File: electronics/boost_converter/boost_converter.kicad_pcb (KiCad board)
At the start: 2 copper layers, 75 x 40 mm, 30 parts, among them J1 Screw_Terminal_01x02, J2 Conn_01x04_Pin, J3 Screw_Terminal_01x02, U1 MC34063AP

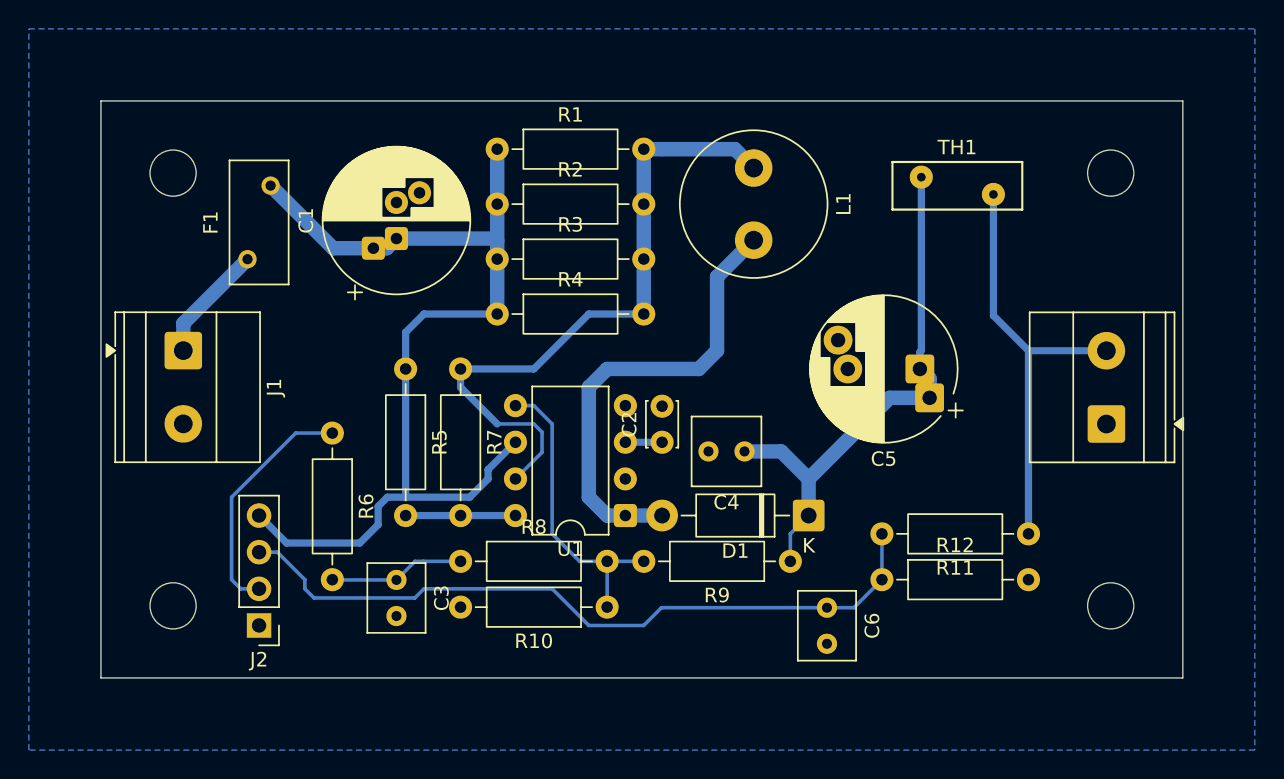
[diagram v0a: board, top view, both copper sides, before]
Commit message: silk screen optimized; drc ok
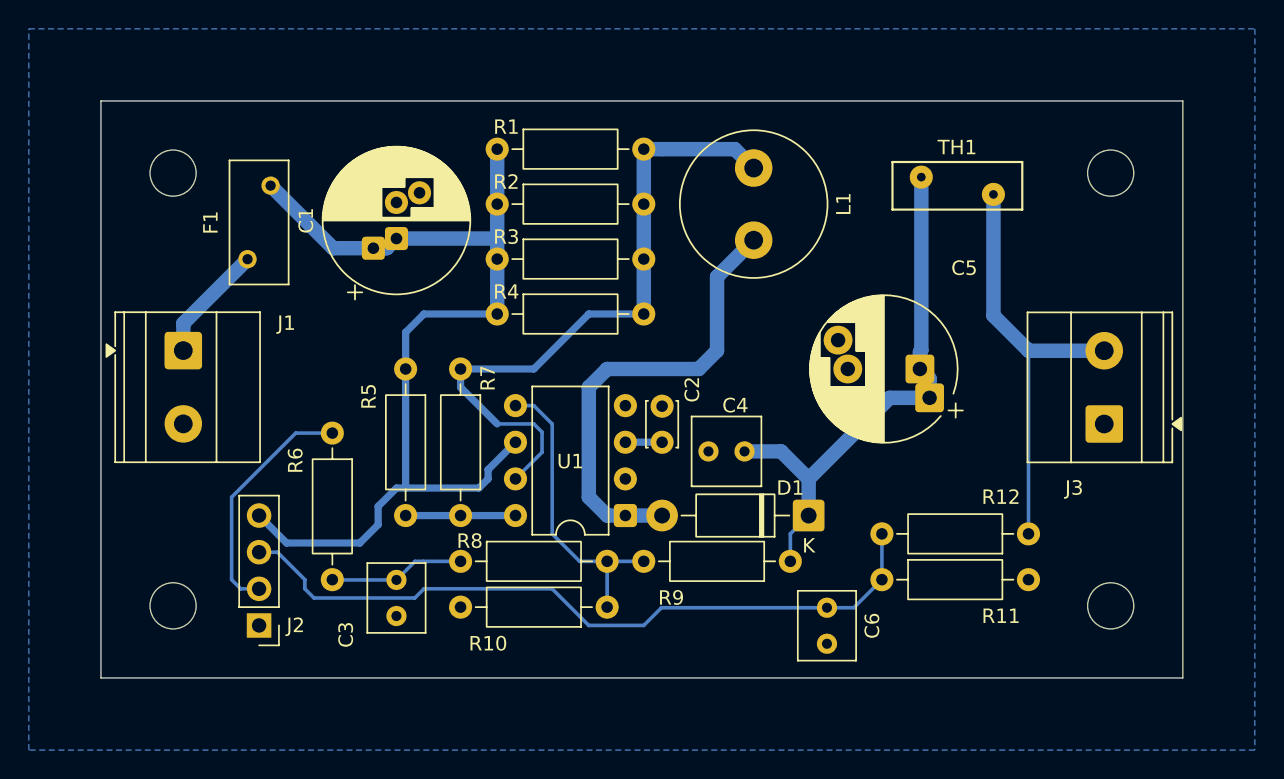
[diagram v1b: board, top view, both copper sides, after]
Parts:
- moved J3 0.15 mm to (119.6, 72.4)
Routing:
- net VCC: track 70.2 -> 69.5 mm
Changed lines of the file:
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@@
 		(tags "Resistor Axial_DIN0207 series Axial Horizontal pin pitch 10.16mm 0.25W = 1/4W length 6.3mm diameter 2.5mm")
 		(property "Reference" "R10"
-			(at 5.08 -2.37 0)
+			(at 8.255 -2.54 0)
 			(layer "F.SilkS")
 			(effects
@@
 		(tags "Resistor Axial_DIN0207 series Axial Horizontal pin pitch 10.16mm 0.25W = 1/4W length 6.3mm diameter 2.5mm")
 		(property "Reference" "R1"
-			(at 5.08 -2.37 0)
+			(at 0.635 -1.524 0)
 			(layer "F.SilkS")
 			(effects
@@
 		(tags "Resistor Axial_DIN0207 series Axial Horizontal pin pitch 10.16mm 0.25W = 1/4W length 6.3mm diameter 2.5mm")
 		(property "Reference" "R9"
-			(at 5.08 -2.37 0)
+			(at 8.255 -2.54 0)
 			(layer "F.SilkS")
 			(effects
@@
 		(tags "Resistor Axial_DIN0207 series Axial Horizontal pin pitch 10.16mm 0.25W = 1/4W length 6.3mm diameter 2.5mm")
 		(property "Reference" "R7"
-			(at 5.08 -2.37 90)
+			(at 0.635 -1.905 90)
 			(layer "F.SilkS")
 			(effects
@@
 		(tags "Resistor Axial_DIN0207 series Axial Horizontal pin pitch 10.16mm 0.25W = 1/4W length 6.3mm diameter 2.5mm")
 		(property "Reference" "R8"
-			(at 5.08 -2.37 0)
+			(at 0.635 -1.397 0)
 			(layer "F.SilkS")
 			(effects
@@
 		(tags "C Rect series Radial pin pitch 2.50mm length 4.6mm width 4.6mm Capacitor")
 		(property "Reference" "C4"
-			(at 1.25 -3.55 180)
+			(at 0.635 3.175 180)
 			(layer "F.SilkS")
 			(effects
@@
 		(tags "Resistor Axial_DIN0207 series Axial Horizontal pin pitch 10.16mm 0.25W = 1/4W length 6.3mm diameter 2.5mm")
 		(property "Reference" "R11"
-			(at 5.08 -2.37 0)
+			(at 1.905 -5.715 0)
 			(layer "F.SilkS")
 			(effects
@@
 		(tags "Resistor Axial_DIN0207 series Axial Horizontal pin pitch 10.16mm 0.25W = 1/4W length 6.3mm diameter 2.5mm")
 		(property "Reference" "R5"
-			(at 5.08 -2.37 90)
+			(at 1.905 2.54 90)
 			(layer "F.SilkS")
 			(effects
@@
 		(tags "Diode DO-41_SOD81 series Axial Horizontal pin pitch 10.16mm  length 5.2mm diameter 2.7mm")
 		(property "Reference" "D1"
-			(at 5.08 -2.47 0)
+			(at 1.27 1.905 0)
 			(layer "F.SilkS")
 			(effects
@@
 		(tags "Resistor Axial_DIN0207 series Axial Horizontal pin pitch 10.16mm 0.25W = 1/4W length 6.3mm diameter 2.5mm")
 		(property "Reference" "R4"
-			(at 5.08 -2.37 0)
+			(at 0.635 -1.524 0)
 			(layer "F.SilkS")
 			(effects
@@
 		(tags "THT DIP DIL PDIP 2.54mm 7.62mm 300mil")
 		(property "Reference" "U1"
-			(at 3.81 -2.33 0)
+			(at 3.81 3.74 0)
 			(layer "F.SilkS")
 			(effects
@@
 		(tags "Resistor Axial_DIN0207 series Axial Horizontal pin pitch 10.16mm 0.25W = 1/4W length 6.3mm diameter 2.5mm")
 		(property "Reference" "R6"
-			(at 5.08 -2.37 90)
+			(at 1.905 2.54 90)
 			(layer "F.SilkS")
 			(effects
@@
 		(tags "THT Terminal Block Phoenix MKDS-1,5-2-5.08 pitch 5.08mm size 10.2x9.8mm drill 1.3mm pad 2.6mm")
 		(property "Reference" "J1"
-			(at 2.54 -6.32 90)
+			(at -1.9 -7.1575 180)
 			(layer "F.SilkS")
 			(effects
@@
 	(footprint "TerminalBlock_Phoenix:TerminalBlock_Phoenix_MKDS-1,5-2-5.08_1x02_P5.08mm_Horizontal"
 		(layer "F.Cu")
-		(at 119.7025 72.395 90)
+		(at 119.5525 72.395 90)
 		(descr "Terminal Block Phoenix MKDS-1,5-2-5.08, 2 pins, pitch 5.08mm, size 10.2x9.8mm, drill diameter 1.3mm, pad diameter 2.6mm, http://www.farnell.com/datasheets/100425.pdf, script-generated using https://gitlab.com/kicad/libraries/kicad-footprint-generator/-/tree/master/scripts/TerminalBlock_Phoenix")
 		(tags "THT Terminal Block Phoenix MKDS-1,5-2-5.08 pitch 5.08mm size 10.2x9.8mm drill 1.3mm pad 2.6mm")
 		(property "Reference" "J3"
-			(at 2.54 -6.32 90)
+			(at -4.44 -2.0775 180)
 			(layer "F.SilkS")
-			(hide yes)
 			(effects
 				(font
@@
 		)
 		(fp_text user "${REFERENCE}"
-			(at 2.54 3.2 90)
+			(at 2.545 1.7325 180)
 			(layer "F.Fab")
 			(effects
@@
 		(tags "C Disc series Radial pin pitch 2.50mm diameter 3mm width 2mm Capacitor")
 		(property "Reference" "C2"
-			(at 1.25 -2.25 90)
+			(at 3.66 2.1 90)
 			(layer "F.SilkS")
 			(effects
@@
 		(tags "Resistor Axial_DIN0207 series Axial Horizontal pin pitch 10.16mm 0.25W = 1/4W length 6.3mm diameter 2.5mm")
 		(property "Reference" "R12"
-			(at 5.08 -2.37 0)
+			(at 8.255 -5.715 0)
 			(layer "F.SilkS")
 			(effects
@@
 		(tags "Resistor Axial_DIN0207 series Axial Horizontal pin pitch 10.16mm 0.25W = 1/4W length 6.3mm diameter 2.5mm")
 		(property "Reference" "R2"
-			(at 5.08 -2.37 0)
+			(at 0.635 -1.524 0)
 			(layer "F.SilkS")
 			(effects
@@
 		(tags "CP Radial series Radial pin pitch 5.00mm 7.50mm diameter 10mm height 16mm Electrolytic Capacitor")
 		(property "Reference" "C5"
-			(at 2.5 -6.25 0)
+			(at -3.082323 6.985 0)
 			(layer "F.SilkS")
 			(effects
@@
 		(tags "C Rect series Radial pin pitch 2.50mm length 4.6mm width 3.8mm Capacitor")
 		(property "Reference" "C3"
-			(at 1.25 -3.15 90)
+			(at 3.795 3.485 90)
 			(layer "F.SilkS")
 			(effects
@@
 		(tags "Through hole pin header THT 1x04 2.54mm single row")
 		(property "Reference" "J2"
-			(at 0 -2.38 0)
+			(at -2.54 0 0)
 			(layer "F.SilkS")
 			(effects
@@
 		(tags "Resistor Axial_DIN0207 series Axial Horizontal pin pitch 10.16mm 0.25W = 1/4W length 6.3mm diameter 2.5mm")
 		(property "Reference" "R3"
-			(at 5.08 -2.37 0)
+			(at 0.635 -1.524 0)
 			(layer "F.SilkS")
 			(effects
@@
 		(start 106.772677 67.402677)
 		(end 106.87 67.305354)
-		(width 0.5)
+		(width 1)
 		(layer "B.Cu")
 		(net 2)
@@
 		(start 106.772677 68.58)
 		(end 106.772677 67.402677)
-		(width 0.5)
+		(width 1)
 		(layer "B.Cu")
 		(net 2)
@@
 		(start 106.87 67.305354)
 		(end 106.87 55.28)
-		(width 0.5)
+		(width 1)
 		(layer "B.Cu")
 		(net 2)
@@
 		(start 111.87 56.48)
 		(end 111.87 64.88)
-		(width 0.5)
+		(width 1)
 		(layer "B.Cu")
 		(net 9)
@@
 	)
 	(segment
-		(start 114.3 80.01)
-		(end 114.3 67.32)
-		(width 0.5)
+		(start 114.305 67.315)
+		(end 119.5525 67.315)
+		(width 1)
 		(layer "B.Cu")
 		(net 9)
 	)
 	(segment
-		(start 114.305 67.315)
-		(end 119.7025 67.315)
-		(width 0.5)
+		(start 114.3 80.01)
+		(end 114.3 67.32)
+		(width 0.25)
 		(layer "B.Cu")
 		(net 9)
@@
 		(start 111.87 64.88)
 		(end 114.305 67.315)
-		(width 0.5)
+		(width 1)
 		(layer "B.Cu")
 		(net 9)
@@
 	)
 	(segment
-		(start 77.47 57.15)
-		(end 77.47 59.69)
-		(width 1)
+		(start 70.485 76.835)
+		(end 69.215 78.105)
+		(width 0.5)
 		(layer "B.Cu")
 		(net 10)
 	)
 	(segment
-		(start 71.12 68.58)
-		(end 71.12 77.47)
-		(width 0.5)
+		(start 77.47 57.15)
+		(end 77.47 59.69)
+		(width 1)
 		(layer "B.Cu")
 		(net 10)
 	)
 	(segment
-		(start 75.565 77.47)
-		(end 71.12 77.47)
+		(start 62.865 80.645)
+		(end 60.96 78.74)
 		(width 0.5)
 		(layer "B.Cu")
@@
 	)
 	(segment
-		(start 71.12 77.47)
-		(end 69.85 77.47)
+		(start 69.215 79.375)
+		(end 67.945 80.645)
 		(width 0.5)
 		(layer "B.Cu")
@@
 	)
 	(segment
-		(start 78.735 73.66)
-		(end 76.835 75.56)
+		(start 71.12 68.58)
+		(end 71.12 76.835)
 		(width 0.5)
 		(layer "B.Cu")
@@
 	)
 	(segment
-		(start 76.835 76.2)
-		(end 75.565 77.47)
-		(width 0.5)
-		(layer "B.Cu")
-		(net 10)
-	)
-	(segment
 		(start 68.885 60.208614)
 		(end 69.814063 60.208614)
@@
 	)
 	(segment
-		(start 69.215 78.105)
-		(end 69.215 79.375)
-		(width 0.5)
-		(layer "B.Cu")
-		(net 10)
-	)
-	(segment
-		(start 69.85 77.47)
-		(end 69.215 78.105)
+		(start 76.835 75.56)
+		(end 78.735 73.66)
 		(width 0.5)
 		(layer "B.Cu")
@@
 	)
 	(segment
-		(start 69.215 79.375)
-		(end 67.945 80.645)
+		(start 71.12 76.835)
+		(end 76.2 76.835)
 		(width 0.5)
 		(layer "B.Cu")
@@
 	)
 	(segment
-		(start 77.47 60.96)
-		(end 77.47 64.77)
-		(width 1)
+		(start 69.215 78.105)
+		(end 69.215 79.375)
+		(width 0.5)
 		(layer "B.Cu")
 		(net 10)
 	)
 	(segment
-		(start 72.39 64.77)
-		(end 71.12 66.04)
+		(start 70.485 76.835)
+		(end 71.12 76.835)
 		(width 0.5)
 		(layer "B.Cu")
@@
 	)
 	(segment
-		(start 62.865 80.645)
-		(end 60.96 78.74)
-		(width 0.5)
+		(start 77.47 60.96)
+		(end 77.47 64.77)
+		(width 1)
 		(layer "B.Cu")
 		(net 10)
 	)
 	(segment
-		(start 76.835 75.56)
-		(end 76.835 76.2)
+		(start 72.39 64.77)
+		(end 71.12 66.04)
 		(width 0.5)
 		(layer "B.Cu")
@@
 	)
 	(segment
-		(start 67.945 80.645)
-		(end 62.865 80.645)
+		(start 76.2 76.835)
+		(end 76.835 76.2)
 		(width 0.5)
 		(layer "B.Cu")
@@
 	)
 	(segment
+		(start 76.835 76.2)
+		(end 76.835 75.56)
+		(width 0.5)
+		(layer "B.Cu")
+		(net 10)
+	)
+	(segment
 		(start 77.47 59.69)
 		(end 77.47 60.96)
@@
 		(layer "B.Cu")
 		(net 10)
+	)
+	(segment
+		(start 67.945 80.645)
+		(end 62.865 80.645)
+		(width 0.5)
+		(layer "B.Cu")
+		(net 10)

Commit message: Labels added; ready for production
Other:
- board text added: "2026-02-10"
- board text added: "Boost Converter"
- board text added: "V.1.0"
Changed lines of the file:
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@@
 		(tags "varistor SIOV")
 		(property "Reference" "TH1"
-			(at 2.5 3.25 0)
+			(at 9 1.235 0)
 			(layer "F.SilkS")
 			(effects
@@
 		)
 		(property "Value" "MountingHole"
-			(at 0 4.15 0)
+			(at 0 -3.565 0)
 			(layer "F.Fab")
 			(effects
@@
 		(layer "F.CrtYd")
 	)
+	(gr_text "Boost Converter"
+		(at 104.775 52.705 0)
+		(layer "F.SilkS")
+		(effects
+			(font
+				(size 1 1)
+				(thickness 0.1)
+			)
+			(justify left bottom)
+		)
+	)
+	(gr_text "V.1.0"
+		(at 113.03 61.595 0)
+		(layer "F.SilkS")
+		(effects
+			(font
+				(size 1 1)
+				(thickness 0.1)
+			)
+			(justify left bottom)
+		)
+	)
+	(gr_text "2026-02-10"
+		(at 113.03 63.5 0)
+		(layer "F.SilkS")
+		(effects
+			(font
+				(size 1 1)
+				(thickness 0.1)
+			)
+			(justify left bottom)
+		)
+	)
 	(segment
